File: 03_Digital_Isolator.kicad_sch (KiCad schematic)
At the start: 1 part, among them IC1 ISO6762DWR

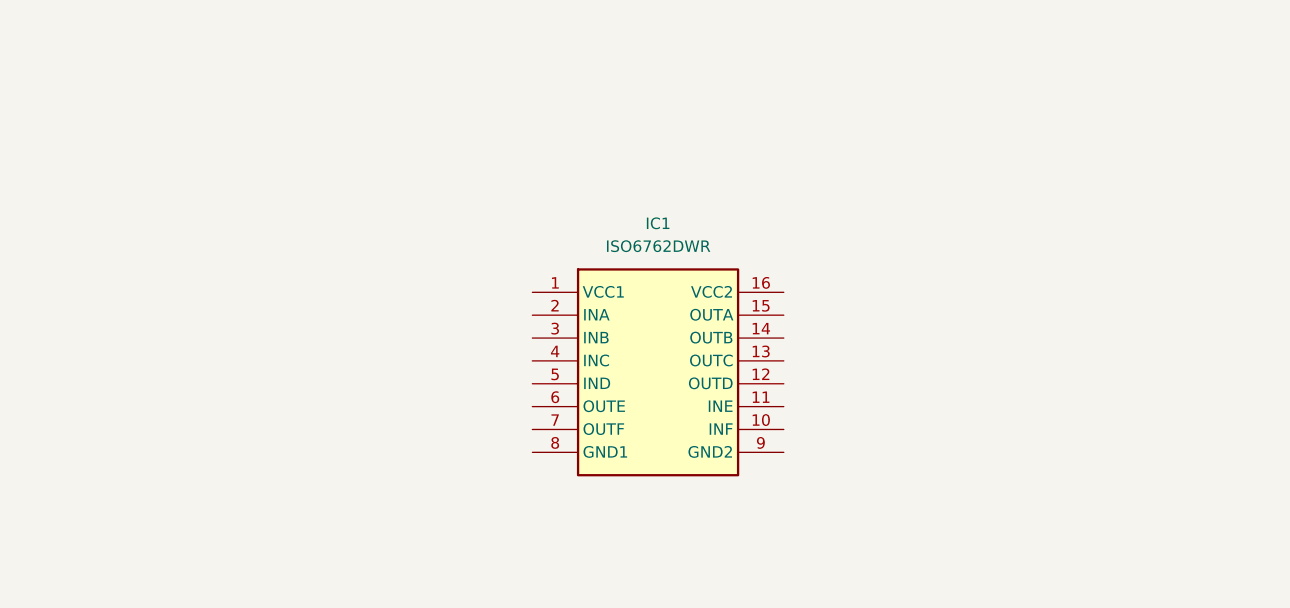
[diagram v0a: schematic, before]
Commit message: completed schematic design, and selected all footprints and for now will go for 0805 for resistors, capacitors and leds - will later make a call during layoting
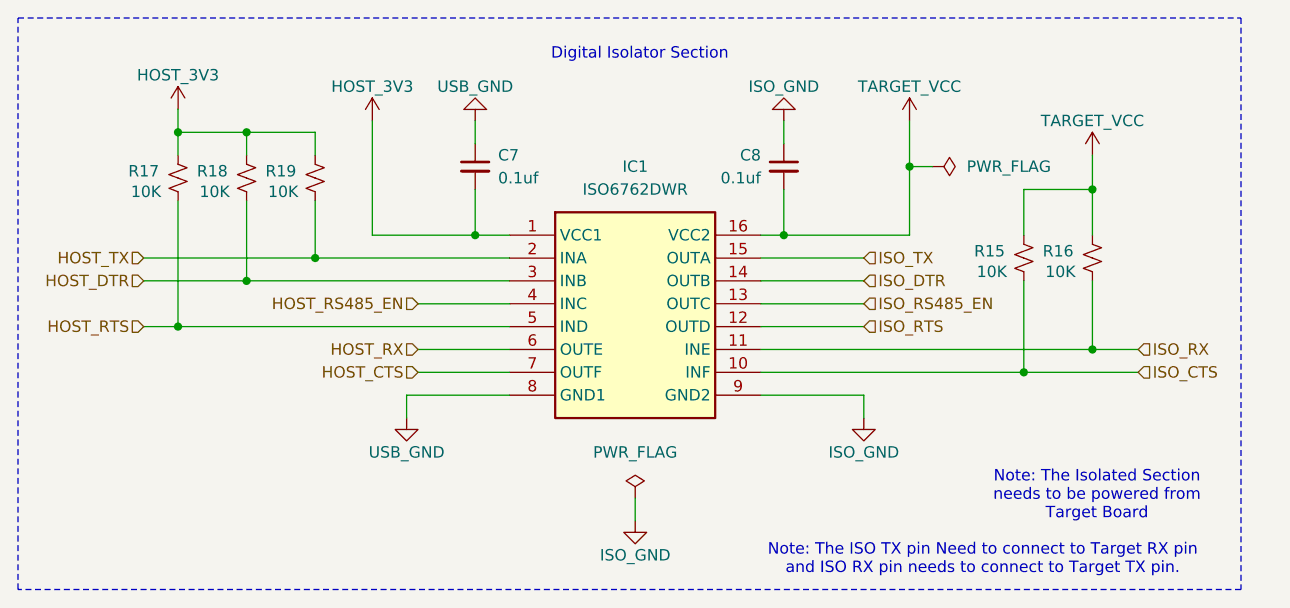
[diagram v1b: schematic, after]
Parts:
- added C7, C8: 0.1uf, Capacitor_SMD:C_0805_2012Metric_Pad1.18x1.45mm_HandSolder, symbol Device:C_Small
- added R15, R16, R17, R18, R19: 10K, Resistor_SMD:R_0805_2012Metric_Pad1.20x1.40mm_HandSolder, symbol Device:R_Small_US
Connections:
- net HOST_3V3: now reaches IC1.1 (VCC1)
- net HOST_3V3: now also C7.2, R17.2, R18.2, R19.2
- net ISO_CTS: now reaches IC1.10 (INF)
- net ISO_CTS: now also R15.1
- net ISO_RX: now reaches IC1.11 (INE)
- net ISO_RX: now also R16.1
- net ISO_RTS: now reaches IC1.12 (OUTD)
- net ISO_RS485_EN: now reaches IC1.13 (OUTC)
- net ISO_DTR: now reaches IC1.14 (OUTB)
- net ISO_TX: now reaches IC1.15 (OUTA)
- net TARGET_VCC: now reaches IC1.16 (VCC2)
- net TARGET_VCC: now also C8.2, R15.2, R16.2
- net HOST_TX: now reaches IC1.2 (INA)
- net HOST_TX: now also R19.1
- net HOST_DTR: now reaches IC1.3 (INB)
- net HOST_DTR: now also R18.1
- net HOST_RS485_EN: now reaches IC1.4 (INC)
- net HOST_RTS: now reaches IC1.5 (IND)
- net HOST_RTS: now also R17.1
- net HOST_RX: now reaches IC1.6 (OUTE)
- net HOST_CTS: now reaches IC1.7 (OUTF)
- net USB_GND: now reaches IC1.8 (GND1)
- net USB_GND: now also C7.1
- net ISO_GND: now reaches IC1.9 (GND2)
- net ISO_GND: now also C8.1
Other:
- note added: "Digital Isolator Section"
- note added: "Note: The ISO TX pin Need to connect to Target RX pin and ISO RX pin needs to connect to Target TX pin."
- note added: "Note: The Isolated Section needs to be powered from Target Board"
- moved on the sheet: IC1
